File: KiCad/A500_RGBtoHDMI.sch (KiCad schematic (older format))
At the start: 5 parts, among them J1 Conn_02x20_Odd_Even, J2 Conn_01x06, U1 Denise_Socket, U2 XC9572XL-VQ64, U3 Denise_MB_PinHeader

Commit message: more routing and fixes
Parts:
- J1: symbol Connector_Generic:Conn_02x20_Odd_Even -> A500_RGBtoHDMI:RPi_Zero_Conn_02x20_Odd_Even
- renumbered J2 to JTAG1
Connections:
- net CBL is gone; now on net CSYNC: U1.32 (BLANK), U3.32 (BLANK)
- net GPIO10 is gone; now on net R0_3V3: J1.19 (GPIO10)
- net GPIO11 is gone; now on net R1_3V3: J1.23 (GPIO11)
- net GPIO12 is gone; now on net R2_3V3: J1.32 (GPIO12)
- net GPIO13 is gone; now on net R3_3V3: J1.33 (GPIO13)
- net GPIO17 is gone; now on net PSYNC: J1.11 (GPIO17)
- net GPIO18 is gone; now on net VERSION: J1.12 (GPIO18)
- net GPIO2 is gone; now on net B0_3V3: J1.3 (GPIO2)
- net GPIO20 is gone; now on net SPCLK: J1.38 (GPIO20)
- net GPIO21 is gone; now on net CLK: J1.40 (GPIO21)
- net GPIO23 is gone; now on net CSYNC_3V3: J1.16 (GPIO23)
- net GPIO3 is gone; now on net B1_3V3: J1.5 (GPIO3)
- net GPIO4 is gone; now on net B2_3V3: J1.7 (GPIO4)
- net GPIO5 is gone; now on net B3_3V3: J1.29 (GPIO5)
- net GPIO6 is gone; now on net G0_3V3: J1.31 (GPIO6)
- net GPIO7 is gone; now on net G1_3V3: J1.26 (GPIO7)
- net GPIO8 is gone; now on net G2_3V3: J1.24 (GPIO8)
- net GPIO9 is gone; now on net G3_3V3: J1.21 (GPIO9)
- net B0: now also U2.56 (FB4-15)
- net B1: now also U2.57 (FB4-17)
- net B2: now also U2.58 (FB2-3)
- net B3: now also U2.59 (FB2-4)
- net G0: now also U2.60 (FB2-2)
- net G1: now also U2.61 (FB2-5)
- net G2: now also U2.62 (FB2-6)
- net G3: now also U2.63 (FB2-8)
- net R0: now also U2.49 (FB4-6)
- net R1: now also U2.50 (FB4-14)
- net R2: now also U2.51 (FB4-10)
- net R3: now also U2.52 (FB4-12)
- net B0_3V3: now reaches U2.1 (FB2-10)
- net B3_3V3: now reaches U2.10 (FB1-6)
- net G0_3V3: now reaches U2.11 (FB1-8)
- net G2_3V3: now reaches U2.12 (FB1-3)
- net G1_3V3: now reaches U2.13 (FB1-4)
- net CLK: now reaches U2.15 (FB1-9/GCK1)
- net SPCLK: now reaches U2.16 (FB1-11/GCK2)
- net CSYNC: now reaches U2.17 (FB1-14/GCK3)
- net R2_3V3: now reaches U2.18 (FB1-10)
- net R3_3V3: now reaches U2.19 (FB1-15)
- net B1_3V3: now reaches U2.2 (FB2-11/GTS2)
- net B2_3V3: now reaches U2.4 (FB2-12)
- net PSYNC: now reaches U2.5 (FB2-14/GTS1)
- net CSYNC_3V3: now reaches U2.6 (FB2-15)
- net VERSION: now reaches U2.64 (FB2-9/GSR)
- net R0_3V3: now reaches U2.7 (FB2-17)
- net G3_3V3: now reaches U2.8 (FB1-2)
- net R1_3V3: now reaches U2.9 (FB1-5)
- net GPIO0: no longer names the net of J1.27 (GPIO0)
- net GPIO1: no longer names the net of J1.28 (GPIO1)
- net GPIO14: no longer names the net of J1.8 (GPIO14)
- net GPIO15: no longer names the net of J1.10 (GPIO15)
- net GPIO16: no longer names the net of J1.36 (GPIO16)
- net GPIO19: no longer names the net of J1.35 (GPIO19)
- net GPIO22: no longer names the net of J1.15 (GPIO22)
- net GPIO24: no longer names the net of J1.18 (GPIO24)
- net GPIO25: no longer names the net of J1.22 (GPIO25)
- net GPIO26: no longer names the net of J1.37 (GPIO26)
- net GPIO27: no longer names the net of J1.13 (GPIO27)
- net ZD renamed PIXELSW
- no-connect marks 2 -> 13
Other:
- moved on the sheet: J1

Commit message: more routing and small adjustments,fixes and improvements
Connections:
- net TCK is gone; now on net TCK_SPCLK: JTAG1.4 (Pin_4), U2.30 (TCK)
- net TDI is gone; now on net TDI_SPDATA: JTAG1.2 (Pin_2), U2.28 (TDI)
- net TMS is gone; now on net TMS_CLKEN: JTAG1.1 (Pin_1), U2.29 (TMS)
- net TDO: now also J1.18 (GPIO24)
- net TDI_SPDATA: now reaches J1.27 (GPIO0)
- net TDI_SPDATA: now also U2.27 (FB3-9)
- net TMS_CLKEN: now reaches J1.28 (GPIO1)
- net TMS_CLKEN: now also U2.31 (FB3-3)
- net PSYNC renamed Pi_CLK
- net SPCLK renamed TCK_SPCLK
- no-connect marks 13 -> 10
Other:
- moved on the sheet: J1, JTAG1, U2

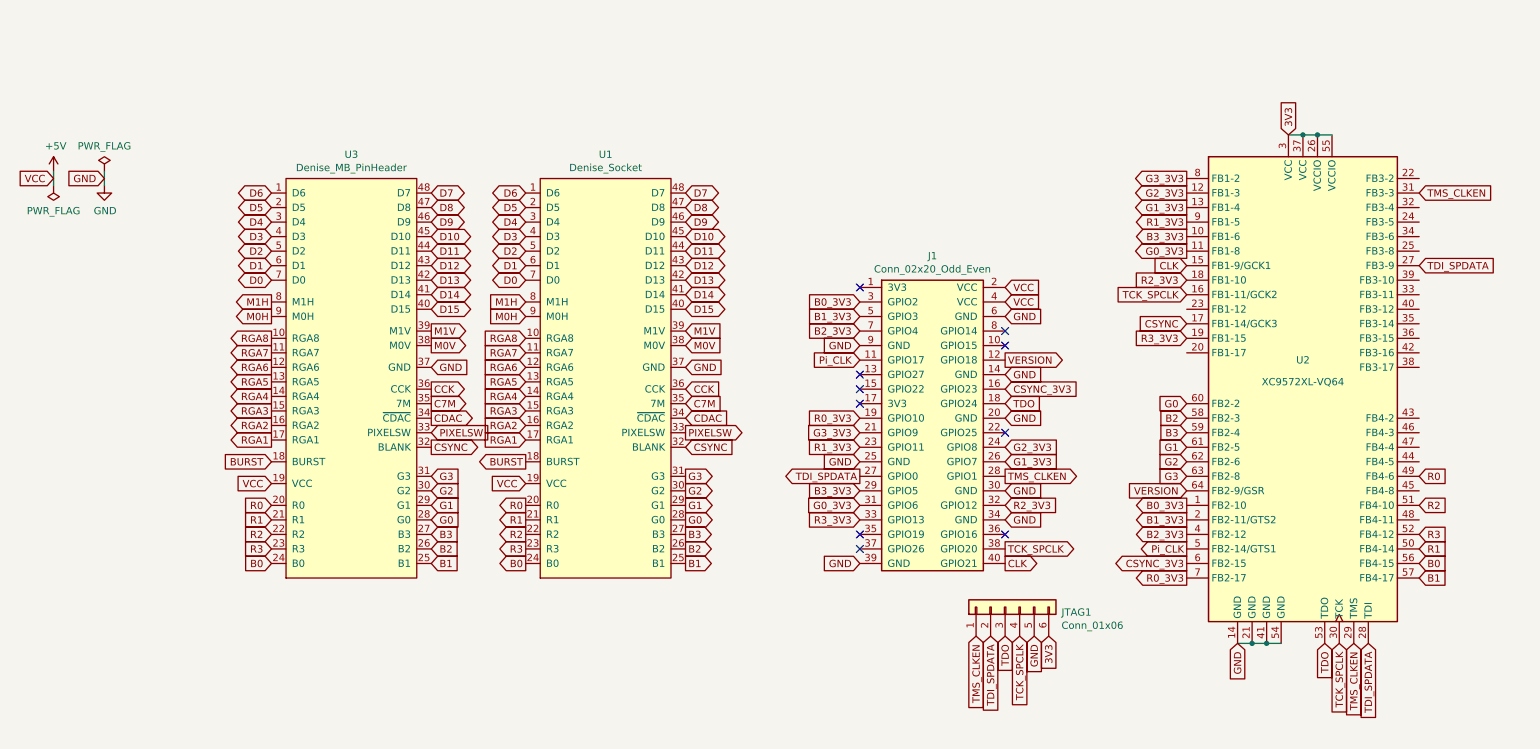
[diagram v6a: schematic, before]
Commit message: added LDO LM1117 3.3V fixed output
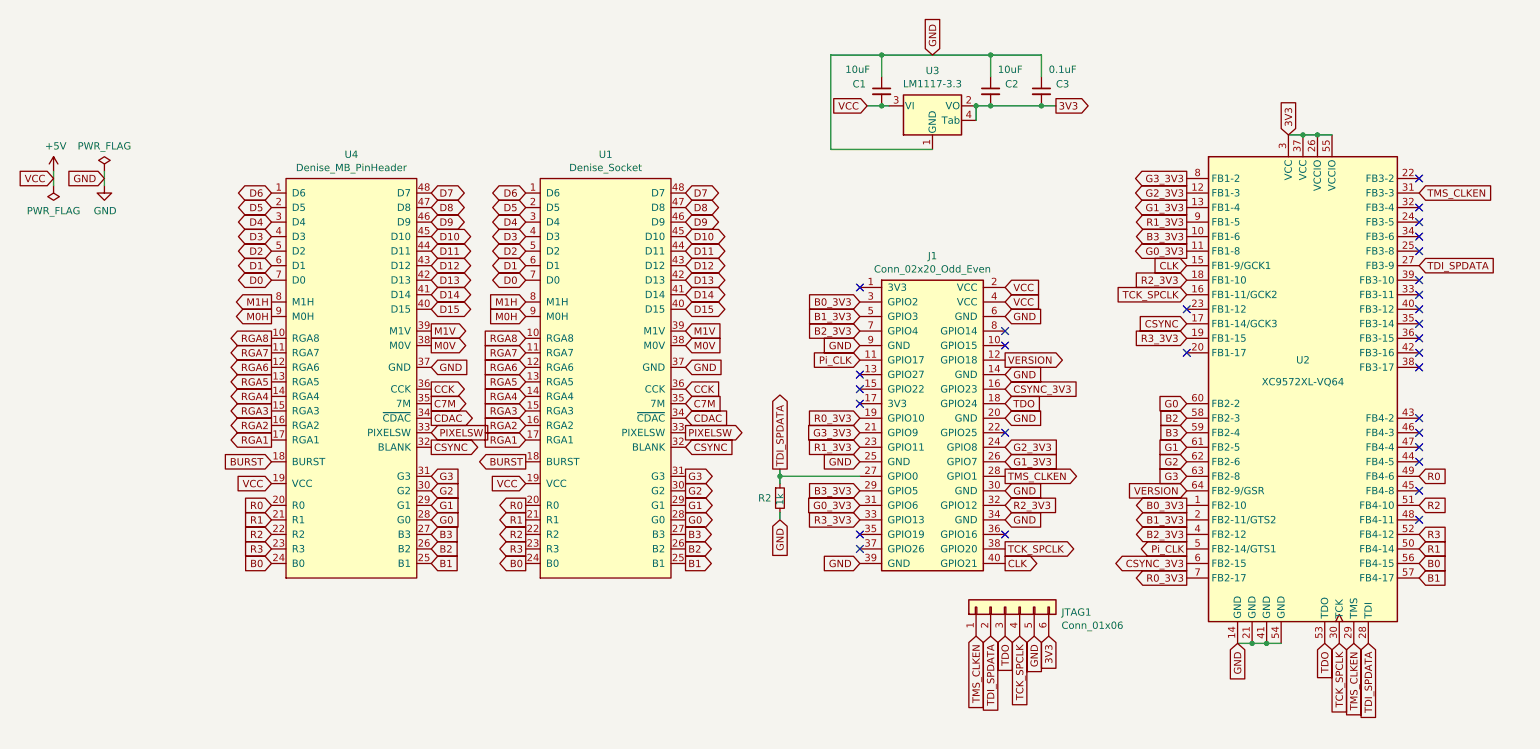
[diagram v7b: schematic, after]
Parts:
- added C1, C2: 10uF, Capacitor_SMD:C_1206_3216Metric_Pad1.42x1.75mm_HandSolder, symbol Device:C_Small
- added C3: 0.1uF, Capacitor_SMD:C_0805_2012Metric_Pad1.15x1.40mm_HandSolder, symbol Device:C_Small
- added R2: 1k, Resistor_SMD:R_0805_2012Metric_Pad1.15x1.40mm_HandSolder, symbol Device:R_Small
- added U3: LM1117-3.3, Package_TO_SOT_SMD:SOT-223, symbol A500_RGBtoHDMI:LM1117-3.3
- renumbered U3 to U4
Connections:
- net +5V: now also C1.2, U3.3 (VI)
- net 3V3: now also C2.2, C3.2, U3.2 (VO), U3.4 (Tab)
- net GND: now also C1.1, C2.1, C3.1, R2.2, U3.1 (GND)
- net TDI_SPDATA: now also R2.1
- no-connect marks 10 -> 30
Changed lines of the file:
@@
 $EndComp
 $Comp
-L A500_RGBtoHDMI:Denise U3
+L A500_RGBtoHDMI:Denise U4
 U 1 1 623BE5C5
 P 2950 3100
-F 0 "U3" H 2950 4665 50  0000 C CNN
+F 0 "U4" H 2950 4665 50  0000 C CNN
 F 1 "Denise_MB_PinHeader" H 2950 4574 50  0000 C CNN
 F 2 "Package_DIP:DIP-48_W15.24mm_LongPads" H 2900 1600 50  0001 C CNN
@@
 Text GLabel 7450 3250 2    50   Input ~ 0
 TDO
-Text GLabel 6450 3750 0    50   Output ~ 0
+Text GLabel 5900 3700 1    50   Output ~ 0
 TDI_SPDATA
 Text GLabel 7350 4850 3    50   Input ~ 0
@@
 Text GLabel 8700 2500 0    50   Input ~ 0
 TCK_SPCLK
+NoConn ~ 8700 2600
+NoConn ~ 8700 2900
+NoConn ~ 10300 1700
+NoConn ~ 10300 1900
+NoConn ~ 10300 2000
+NoConn ~ 10300 2100
+NoConn ~ 10300 2200
+NoConn ~ 10300 2400
+NoConn ~ 10300 2500
+NoConn ~ 10300 2600
+NoConn ~ 10300 2700
+NoConn ~ 10300 2800
+NoConn ~ 10300 2900
+NoConn ~ 10300 3000
+NoConn ~ 10300 3350
+NoConn ~ 10300 3450
+NoConn ~ 10300 3550
+NoConn ~ 10300 3650
+NoConn ~ 10300 3850
+NoConn ~ 10300 4050
+$Comp
+L A500_RGBtoHDMI:LM1117-3.3 U3
+U 1 1 6246B1F1
+P 6950 1200
+F 0 "U3" H 6950 1442 50  0000 C CNN
+F 1 "LM1117-3.3" H 6950 1351 50  0000 C CNN
+F 2 "Package_TO_SOT_SMD:SOT-223" H 6950 1200 50  0001 C CNN
+F 3 "http://www.ti.com/lit/ds/symlink/lm1117.pdf" H 6950 1200 50  0001 C CNN
+	1    6950 1200
+	1    0    0    -1
+$EndComp
+Text GLabel 6500 1200 0    50   Input ~ 0
+VCC
+Text GLabel 6950 850  1    50   Input ~ 0
+GND
+Wire Wire Line
+	6950 1500 6250 1500
+Wire Wire Line
+	6250 1500 6250 850
+Wire Wire Line
+	7250 1300 7250 1200
+Wire Wire Line
+	7250 1200 7350 1200
+Connection ~ 7250 1200
+Text GLabel 7800 1200 2    50   Output ~ 0
+3V3
+$Comp
+L Device:C_Small C1
+U 1 1 6246F468
+P 6600 1100
+F 0 "C1" H 6400 1150 50  0000 L CNN
+F 1 "10uF" H 6350 1250 50  0000 L CNN
+F 2 "Capacitor_SMD:C_1206_3216Metric_Pad1.42x1.75mm_HandSolder" H 6600 1100 50  0001 C CNN
+F 3 "~" H 6600 1100 50  0001 C CNN
+	1    6600 1100
+	1    0    0    -1
+$EndComp
+Wire Wire Line
+	6250 850  6600 850
+Connection ~ 6600 1200
+Wire Wire Line
+	6600 1200 6650 1200
+Wire Wire Line
+	6500 1200 6600 1200
+Wire Wire Line
+	6600 1000 6600 850
+Connection ~ 6600 850
+$Comp
+L Device:C_Small C2
+U 1 1 62473099
+P 7350 1100
+F 0 "C2" H 7450 1150 50  0000 L CNN
+F 1 "10uF" H 7400 1250 50  0000 L CNN
+F 2 "Capacitor_SMD:C_1206_3216Metric_Pad1.42x1.75mm_HandSolder" H 7350 1100 50  0001 C CNN
+F 3 "~" H 7350 1100 50  0001 C CNN
+	1    7350 1100
+	1    0    0    -1
+$EndComp
+Connection ~ 7350 1200
+Wire Wire Line
+	7350 1200 7700 1200
+Wire Wire Line
+	7350 1000 7350 850
+Wire Wire Line
+	6600 850  7350 850
+$Comp
+L Device:C_Small C3
+U 1 1 62475F7C
+P 7700 1100
+F 0 "C3" H 7800 1150 50  0000 L CNN
+F 1 "0.1uF" H 7750 1250 50  0000 L CNN
+F 2 "Capacitor_SMD:C_0805_2012Metric_Pad1.15x1.40mm_HandSolder" H 7700 1100 50  0001 C CNN
+F 3 "~" H 7700 1100 50  0001 C CNN
+	1    7700 1100
+	1    0    0    -1
+$EndComp
+Connection ~ 7700 1200
+Wire Wire Line
+	7700 1200 7800 1200
+Wire Wire Line
+	7700 1000 7700 850
+Wire Wire Line
+	7700 850  7350 850
+Connection ~ 7350 850
+$Comp
+L Device:R_Small R2
+U 1 1 624D6906
+P 5900 3900
+F 0 "R2" H 5750 3900 50  0000 L CNN
+F 1 "1k" V 5900 3850 50  0000 L CNN
+F 2 "Resistor_SMD:R_0805_2012Metric_Pad1.15x1.40mm_HandSolder" H 5900 3900 50  0001 C CNN
+F 3 "~" H 5900 3900 50  0001 C CNN
+	1    5900 3900
+	1    0    0    -1
+$EndComp
+Wire Wire Line
+	6450 3750 5900 3750
+Text GLabel 5900 4050 3    50   Input ~ 0
+GND
+Wire Wire Line
+	5900 3700 5900 3750
+Connection ~ 5900 3750
+Wire Wire Line
+	5900 3750 5900 3800
+Wire Wire Line
+	5900 4000 5900 4050
 $EndSCHEMATC

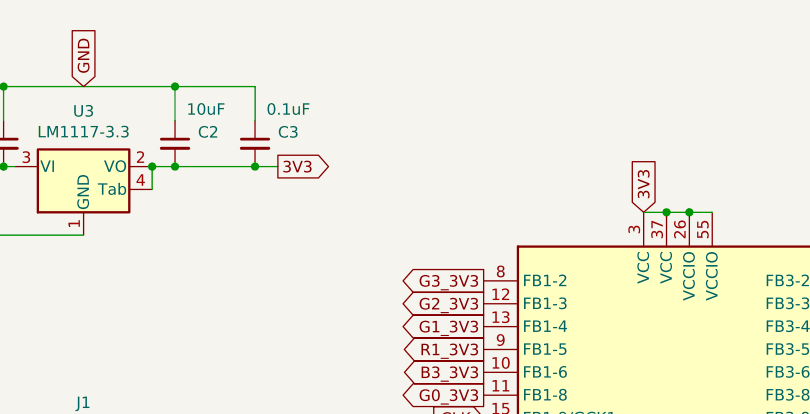
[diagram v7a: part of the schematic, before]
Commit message: added 100nF decoupling caps to CPLDs 3V3-inputs
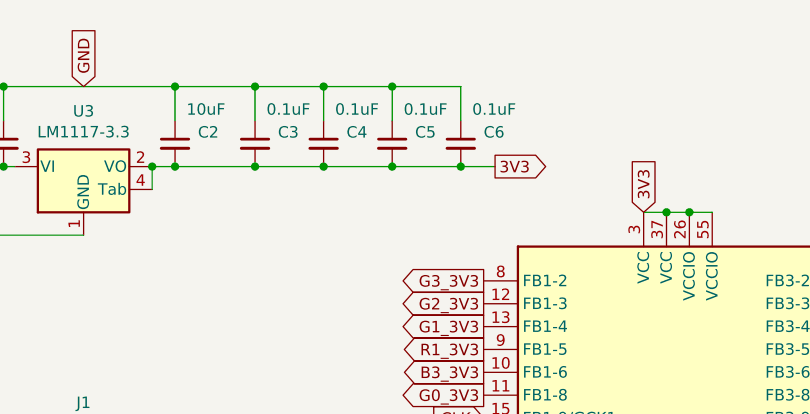
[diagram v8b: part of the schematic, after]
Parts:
- added C4, C5, C6: 0.1uF, Capacitor_SMD:C_0805_2012Metric_Pad1.15x1.40mm_HandSolder, symbol Device:C_Small
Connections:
- net 3V3: now also C4.2, C5.2, C6.2
- net GND: now also C4.1, C5.1, C6.1
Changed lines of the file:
@@
 	7250 1200 7350 1200
 Connection ~ 7250 1200
-Text GLabel 7800 1200 2    50   Output ~ 0
+Text GLabel 8750 1200 2    50   Output ~ 0
 3V3
 $Comp
@@
 Connection ~ 7700 1200
 Wire Wire Line
-	7700 1200 7800 1200
-Wire Wire Line
 	7700 1000 7700 850
 Wire Wire Line
@@
 Wire Wire Line
 	5900 4000 5900 4050
+$Comp
+L Device:C_Small C4
+U 1 1 624DDB45
+P 8000 1100
+F 0 "C4" H 8100 1150 50  0000 L CNN
+F 1 "0.1uF" H 8050 1250 50  0000 L CNN
+F 2 "Capacitor_SMD:C_0805_2012Metric_Pad1.15x1.40mm_HandSolder" H 8000 1100 50  0001 C CNN
+F 3 "~" H 8000 1100 50  0001 C CNN
+	1    8000 1100
+	1    0    0    -1
+$EndComp
+$Comp
+L Device:C_Small C5
+U 1 1 624DE9B4
+P 8300 1100
+F 0 "C5" H 8400 1150 50  0000 L CNN
+F 1 "0.1uF" H 8350 1250 50  0000 L CNN
+F 2 "Capacitor_SMD:C_0805_2012Metric_Pad1.15x1.40mm_HandSolder" H 8300 1100 50  0001 C CNN
+F 3 "~" H 8300 1100 50  0001 C CNN
+	1    8300 1100
+	1    0    0    -1
+$EndComp
+$Comp
+L Device:C_Small C6
+U 1 1 624DF886
+P 8600 1100
+F 0 "C6" H 8700 1150 50  0000 L CNN
+F 1 "0.1uF" H 8650 1250 50  0000 L CNN
+F 2 "Capacitor_SMD:C_0805_2012Metric_Pad1.15x1.40mm_HandSolder" H 8600 1100 50  0001 C CNN
+F 3 "~" H 8600 1100 50  0001 C CNN
+	1    8600 1100
+	1    0    0    -1
+$EndComp
+Wire Wire Line
+	7700 1200 8000 1200
+Connection ~ 8000 1200
+Wire Wire Line
+	8000 1200 8300 1200
+Connection ~ 8300 1200
+Wire Wire Line
+	8300 1200 8600 1200
+Connection ~ 8600 1200
+Wire Wire Line
+	8600 1200 8750 1200
+Wire Wire Line
+	8000 1000 8000 850
+Wire Wire Line
+	8000 850  7700 850
+Connection ~ 7700 850
+Wire Wire Line
+	8300 1000 8300 850
+Wire Wire Line
+	8300 850  8000 850
+Connection ~ 8000 850
+Wire Wire Line
+	8600 1000 8600 850
+Wire Wire Line
+	8600 850  8300 850
+Connection ~ 8300 850
 $EndSCHEMATC
